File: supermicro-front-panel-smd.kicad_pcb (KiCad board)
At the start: 2 copper layers, 24.1 x 31.8 mm, 9 parts

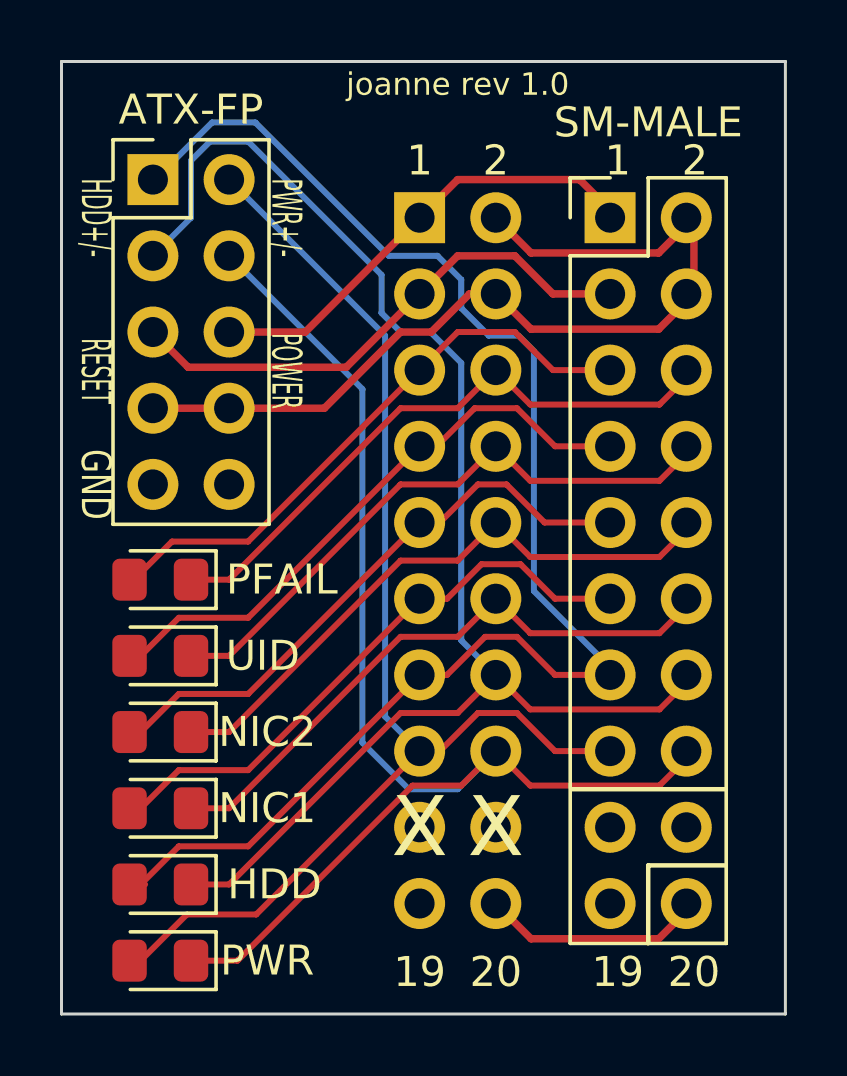
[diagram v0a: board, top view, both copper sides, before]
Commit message: swapped position of male and female headers
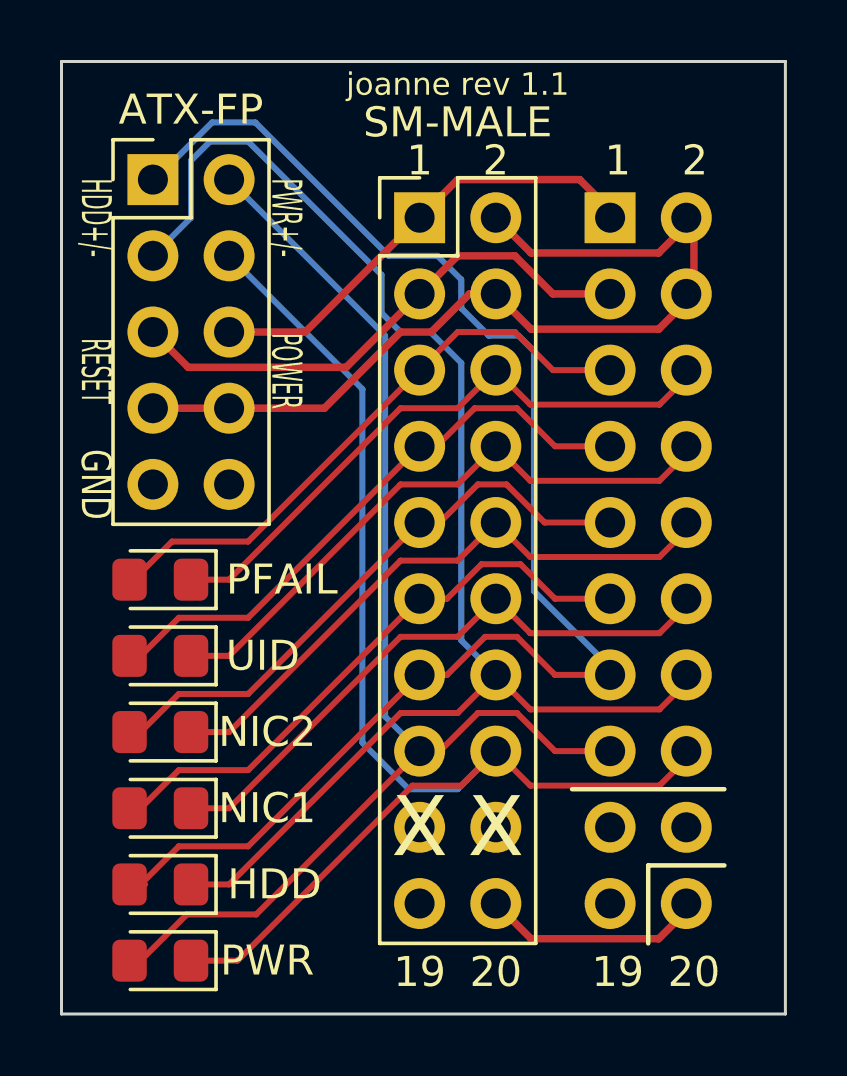
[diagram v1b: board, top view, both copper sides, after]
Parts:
- moved SM-FEMALE 6.35 mm to (119.4, 59.7)
- moved SM-MALE 6.35 mm to (113.0, 59.7)
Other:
- board text added: "joanne rev 1.1"
- board text removed: "joanne rev 1.0"
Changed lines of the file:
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@@
   )
   (footprint "Connector_PinHeader_2.54mm:PinHeader_2x10_P2.54mm_Vertical" (layer "F.Cu")
-    (at 119.38 59.69)
+    (at 113.03 59.69)
     (descr "Through hole straight pin header, 2x10, 2.54mm pitch, double rows")
     (tags "Through hole pin header THT 2x10 2.54mm double row")
@@
   )
   (footprint "Connector_PinSocket_2.54mm:PinSocket_2x10_P2.54mm_Vertical" (layer "B.Cu")
-    (at 113.03 59.69 180)
+    (at 119.38 59.69 180)
     (descr "Through hole straight socket strip, 2x10, 2.54mm pitch, double cols (from Kicad 4.0.7), script generated")
     (tags "Through hole socket strip THT 2x10 2.54mm double row")
@@
     (effects (font (size 1 1) (thickness 0.15)))
   )
-  (gr_text "joanne rev 1.0" (at 114.3 55.245) (layer "F.SilkS")
+  (gr_text "joanne rev 1.1" (at 114.3 55.245) (layer "F.SilkS")
     (effects (font (size 0.75 0.75) (thickness 0.15)))
   )
